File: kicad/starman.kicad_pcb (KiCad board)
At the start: 4 copper layers, 182 x 150 mm, 202 parts, among them J1 Conn_01x12, J10 Barrel_Jack_MountingPin, J2 Conn_01x10, J3 Conn_01x12, J4 Conn_01x06, J5 Conn_02x03_Counter_Clockwise, J6 Conn_01x12, J7 Conn_01x10, J8 Conn_01x12, J9 Conn_01x08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

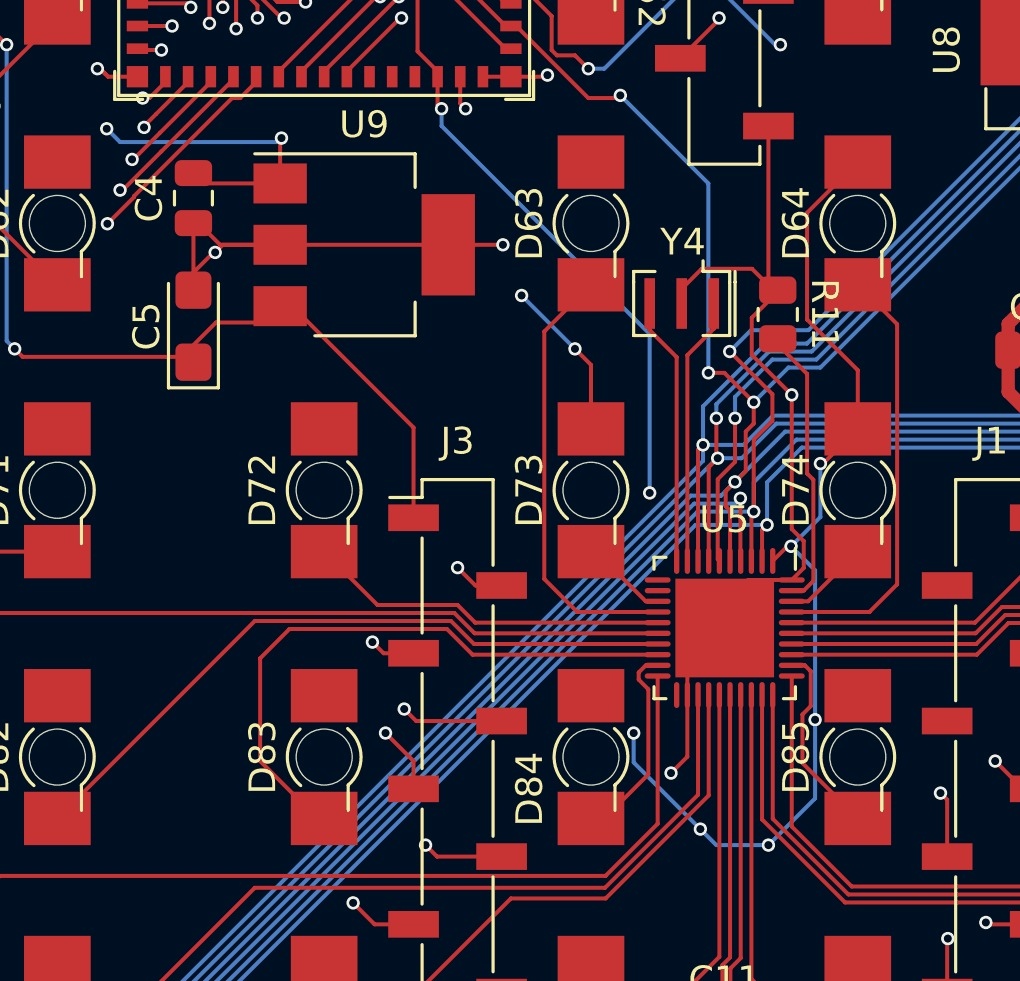
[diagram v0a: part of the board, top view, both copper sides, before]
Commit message: Clean up some +5V routes to be more balanced around D64 and D83
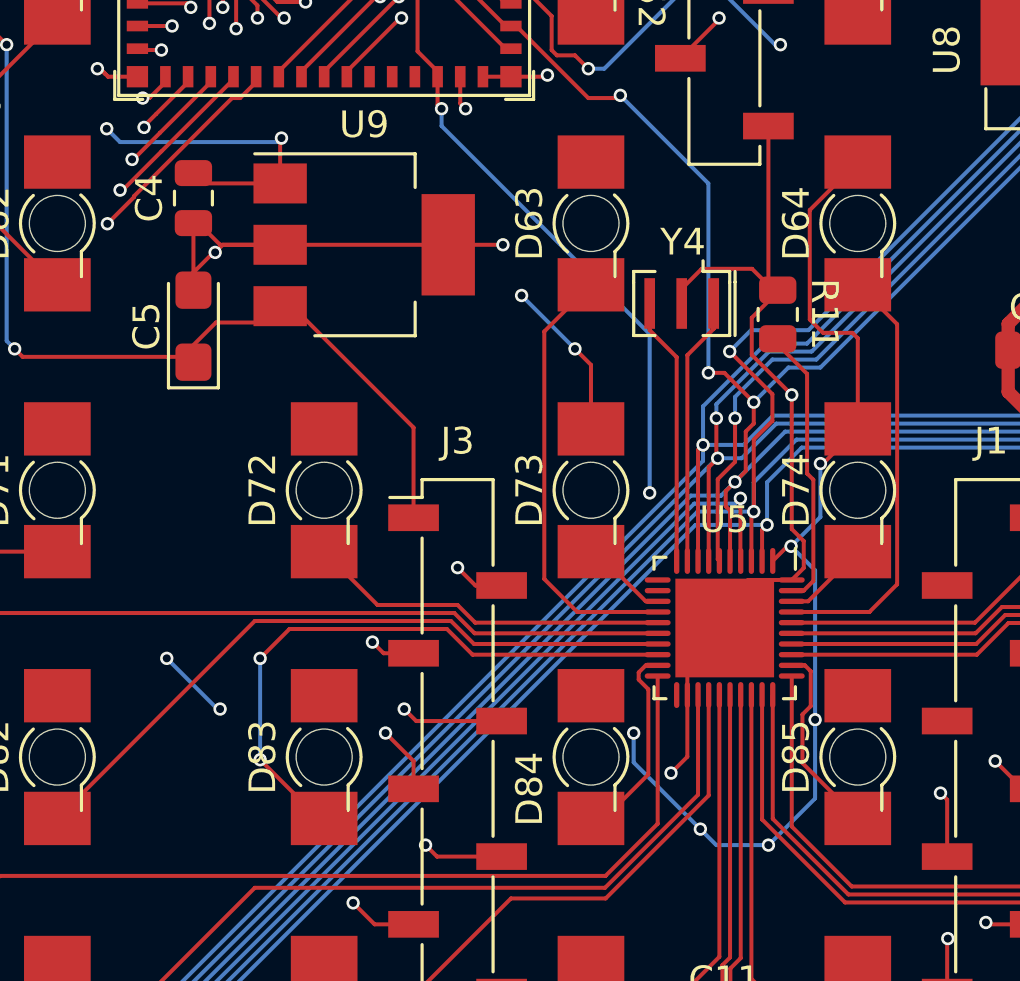
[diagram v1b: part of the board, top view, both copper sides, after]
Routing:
- net +5V: track 248.5 -> 251.9 mm, vias 50 -> 52
- net Net-(D83-Pad1): track 22.9 -> 23.2 mm, vias 0 -> 2
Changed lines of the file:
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@@
   (segment (start 165 152.7) (end 164.5 153.2) (width 0.15) (layer "F.Cu") (net 5))
   (segment (start 105 72.7) (end 106.8 74.5) (width 0.15) (layer "F.Cu") (net 5))
+  (segment (start 113.2 104.5) (end 115 102.7) (width 0.15) (layer "F.Cu") (net 5))
   (segment (start 125 132.7) (end 125 131.45) (width 0.15) (layer "F.Cu") (net 5))
   (segment (start 146.6 87.4) (end 147.3625 88.1625) (width 0.15) (layer "F.Cu") (net 5))
@@
   (segment (start 108.1 73.300794) (end 107.948511 73.452283) (width 0.15) (layer "F.Cu") (net 5))
   (segment (start 85 92.7) (end 83.9 92.7) (width 0.15) (layer "F.Cu") (net 5))
-  (segment (start 113.1 108.6) (end 113.1 104.6) (width 0.15) (layer "F.Cu") (net 5))
-  (segment (start 115 112.7) (end 115 110.5) (width 0.15) (layer "F.Cu") (net 5))
   (segment (start 145 82.7) (end 146.6 84.3) (width 0.15) (layer "F.Cu") (net 5))
   (segment (start 66.6 144.1) (end 65.2 142.7) (width 0.15) (layer "F.Cu") (net 5))
+  (segment (start 115 109.3) (end 114.8 109.1) (width 0.15) (layer "F.Cu") (net 5))
   (segment (start 162.2875 147) (end 161.8 147.4875) (width 0.15) (layer "F.Cu") (net 5))
   (segment (start 80.9875 95.075) (end 80.9875 97.5875) (width 0.15) (layer "F.Cu") (net 5))
@@
   (segment (start 80.9875 94.3125) (end 81.6 93.7) (width 0.15) (layer "F.Cu") (net 5))
   (segment (start 90.4875 103.5) (end 90.1 103.1125) (width 0.15) (layer "F.Cu") (net 5))
+  (segment (start 114.8 109.1) (end 113.7 109.1) (width 0.15) (layer "F.Cu") (net 5))
   (segment (start 61.8 147.1) (end 62.3 146.6) (width 0.15) (layer "F.Cu") (net 5))
   (segment (start 115 112.7) (end 113.7 114) (width 0.15) (layer "F.Cu") (net 5))
@@
   (segment (start 158.8125 95.9875) (end 159.6 95.2) (width 0.15) (layer "F.Cu") (net 5))
   (segment (start 145 82.7) (end 146.1 82.7) (width 0.15) (layer "F.Cu") (net 5))
+  (segment (start 113.2 108.6) (end 113.2 104.5) (width 0.15) (layer "F.Cu") (net 5))
   (segment (start 129.85 109.8) (end 127.54 107.49) (width 0.5) (layer "F.Cu") (net 5))
-  (segment (start 115 110.5) (end 113.1 108.6) (width 0.15) (layer "F.Cu") (net 5))
   (segment (start 93.35 103.5) (end 90.4875 103.5) (width 0.15) (layer "F.Cu") (net 5))
   (segment (start 112.3625 117.1) (end 112.5 117.1) (width 0.15) (layer "F.Cu") (net 5))
   (segment (start 165 92.7) (end 162.3 92.7) (width 0.15) (layer "F.Cu") (net 5))
   (segment (start 105 110.3) (end 104.4 109.7) (width 0.15) (layer "F.Cu") (net 5))
+  (segment (start 113.7 109.1) (end 113.2 108.6) (width 0.15) (layer "F.Cu") (net 5))
   (segment (start 80.9875 95.075) (end 80.9875 94.3125) (width 0.15) (layer "F.Cu") (net 5))
-  (segment (start 113.1 104.6) (end 115 102.7) (width 0.15) (layer "F.Cu") (net 5))
   (segment (start 115 72.7) (end 113.3 72.7) (width 0.15) (layer "F.Cu") (net 5))
+  (segment (start 115 112.7) (end 115 109.3) (width 0.15) (layer "F.Cu") (net 5))
   (segment (start 108.1 72.6625) (end 108.1 73.300794) (width 0.15) (layer "F.Cu") (net 5))
   (segment (start 127.54 107.49) (end 127.54 104.275) (width 0.5) (layer "F.Cu") (net 5))
@@
   (via (at 111.65 128.3) (size 0.5) (drill 0.3) (layers "F.Cu" "B.Cu") (net 5))
   (via (at 118.8 72.9) (size 0.5) (drill 0.3) (layers "F.Cu" "B.Cu") (net 5))
+  (via (at 91.1 123.2) (size 0.5) (drill 0.3) (layers "F.Cu" "B.Cu") (net 5))
   (via (at 162.3 147) (size 0.5) (drill 0.3) (layers "F.Cu" "B.Cu") (net 5))
+  (via (at 89.1 121.3) (size 0.5) (drill 0.3) (layers "F.Cu" "B.Cu") (net 5))
   (via (at 115.734095 79.565905) (size 0.5) (drill 0.3) (layers "F.Cu" "B.Cu") (net 5))
   (via (at 163.5 153.2) (size 0.5) (drill 0.3) (layers "F.Cu" "B.Cu") (net 5))
@@
   (segment (start 118.7 72.8) (end 118.8 72.9) (width 0.15) (layer "B.Cu") (net 5))
   (segment (start 113.2 77.1) (end 115.665905 79.565905) (width 0.15) (layer "B.Cu") (net 5))
+  (segment (start 91 123.2) (end 91.1 123.2) (width 0.15) (layer "B.Cu") (net 5))
   (segment (start 162.3 147) (end 162.3 145.1) (width 0.15) (layer "B.Cu") (net 5))
   (segment (start 82.6255 99.2255) (end 82.6255 100.6) (width 0.15) (layer "B.Cu") (net 5))
@@
   (segment (start 109.1 127.7) (end 106.6 125.2) (width 0.15) (layer "B.Cu") (net 5))
   (segment (start 63.2 157.3) (end 61.3 159.2) (width 0.15) (layer "B.Cu") (net 5))
+  (segment (start 89.1 121.3) (end 91 123.2) (width 0.15) (layer "B.Cu") (net 5))
   (segment (start 111.9 98.3) (end 112.1 98.3) (width 0.15) (layer "B.Cu") (net 5))
   (segment (start 63.2 147.1) (end 63.2 153.1) (width 0.15) (layer "B.Cu") (net 5))
@@
   (segment (start 100.615358 120.7625) (end 99.753347 119.900491) (width 0.15) (layer "F.Cu") (net 88))
   (segment (start 107.5 120.7625) (end 100.615358 120.7625) (width 0.15) (layer "F.Cu") (net 88))
-  (segment (start 92.6 121.3) (end 92.6 125.15) (width 0.15) (layer "F.Cu") (net 89))
-  (segment (start 92.6 125.15) (end 94.75 127.3) (width 0.15) (layer "F.Cu") (net 89))
   (segment (start 94.75 127.3) (end 95 127.3) (width 0.15) (layer "F.Cu") (net 89))
   (segment (start 99.6 120.2) (end 93.7 120.2) (width 0.15) (layer "F.Cu") (net 89))
   (segment (start 107.5 121.1625) (end 100.5625 121.1625) (width 0.15) (layer "F.Cu") (net 89))
+  (segment (start 92.6 125.1) (end 94.8 127.3) (width 0.15) (layer "F.Cu") (net 89))
   (segment (start 100.5625 121.1625) (end 99.6 120.2) (width 0.15) (layer "F.Cu") (net 89))
   (segment (start 93.7 120.2) (end 92.6 121.3) (width 0.15) (layer "F.Cu") (net 89))
+  (segment (start 94.8 127.3) (end 95 127.3) (width 0.15) (layer "F.Cu") (net 89))
+  (via (at 92.6 125.1) (size 0.5) (drill 0.3) (layers "F.Cu" "B.Cu") (net 89))
+  (via (at 92.6 121.3) (size 0.5) (drill 0.3) (layers "F.Cu" "B.Cu") (net 89))
+  (segment (start 92.6 125.1) (end 92.6 125.15) (width 0.15) (layer "B.Cu") (net 89))
+  (segment (start 92.6 121.3) (end 92.6 125.1) (width 0.15) (layer "B.Cu") (net 89))
   (segment (start 107.5 121.5625) (end 107.05356 121.5625) (width 0.15) (layer "F.Cu") (net 90))
   (segment (start 106.78798 121.82808) (end 106.78798 122.09692) (width 0.15) (layer "F.Cu") (net 90))

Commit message: Added KiCad and OSHW logos
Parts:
- J1, J3: value Conn_01x12 -> M20-8771246
- J2: value Conn_01x10 -> M20-8770646
- J4: value Conn_01x06 -> ESW-106-44-T-S
- J6, J8: value Conn_01x12 -> ESW-112-44-T-S
- J9: value Conn_01x08 -> Conn_01x10
- LS1: value Speaker -> CVS 1708
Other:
- board text added: "v2.0"
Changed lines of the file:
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@@
   (net 255 "Net-(R13-Pad2)")
   (net 256 "/ext_SOUND")
-  (net 257 "Net-(RV1-Pad2)")
+  (net 257 "Net-(LS1-Pad2)")
   (net 258 "/SOUND")
   (net 259 "Net-(R4-Pad2)")
@@
       (effects (font (size 1 1) (thickness 0.15)))
     )
-    (fp_text value "Conn_01x12" (at 0 16.84) (layer "F.Fab")
+    (fp_text value "M20-8771246" (at 0 16.84) (layer "F.Fab")
       (effects (font (size 1 1) (thickness 0.15)))
     )
@@
       (effects (font (size 1 1) (thickness 0.15)))
     )
-    (fp_text value "Conn_01x10" (at 0 9.22) (layer "F.Fab")
+    (fp_text value "M20-8770646" (at 0 9.22) (layer "F.Fab")
       (effects (font (size 1 1) (thickness 0.15)))
     )
@@
       (net 256 "/ext_SOUND") (pinfunction "1") (pintype "passive"))
     (pad "2" thru_hole circle (at -2.54 -2.54 90) (size 1.26 1.26) (drill 0.7) (layers *.Cu *.Mask)
-      (net 257 "Net-(RV1-Pad2)") (pinfunction "2") (pintype "passive"))
+      (net 257 "Net-(LS1-Pad2)") (pinfunction "2") (pintype "passive"))
     (pad "3" thru_hole circle (at 0 -5.08 90) (size 1.26 1.26) (drill 0.7) (layers *.Cu *.Mask)
-      (net 263 "unconnected-(RV1-Pad3)") (pinfunction "3") (pintype "passive"))
+      (net 263 "unconnected-(RV1-Pad3)") (pinfunction "3") (pintype "passive+no_connect"))
     (model "${KICAD6_3DMODEL_DIR}/Potentiometer_THT.3dshapes/Potentiometer_Bourns_3339P_Vertical.wrl"
       (offset (xyz 0 0 0))
@@
       (effects (font (size 1 1) (thickness 0.15)))
     )
-    (fp_text value "Conn_01x12" (at 0 16.84) (layer "F.Fab")
+    (fp_text value "M20-8771246" (at 0 16.84) (layer "F.Fab")
       (effects (font (size 1 1) (thickness 0.15)))
     )
@@
       (effects (font (size 1 1) (thickness 0.15)))
     )
-    (fp_text value "Conn_01x08" (at 0 25.19) (layer "F.Fab")
+    (fp_text value "Conn_01x10" (at 0 25.19) (layer "F.Fab")
       (effects (font (size 1 1) (thickness 0.15)))
     )
@@
       (effects (font (size 1 1) (thickness 0.15)))
     )
-    (fp_text value "Speaker" (at 4 9) (layer "F.Fab")
+    (fp_text value "CVS 1708" (at 4 9) (layer "F.Fab")
       (effects (font (size 1 1) (thickness 0.15)))
     )
@@
       (net 234 "GNDA") (pinfunction "1") (pintype "input"))
     (pad "2" thru_hole circle (at 7.61 0 180) (size 1.6002 1.6002) (drill 1.00076) (layers *.Cu *.Mask)
-      (net 257 "Net-(RV1-Pad2)") (pinfunction "2") (pintype "input"))
+      (net 257 "Net-(LS1-Pad2)") (pinfunction "2") (pintype "input"))
     (model "${KICAD6_3DMODEL_DIR}/Buzzer_Beeper.3dshapes/MagneticBuzzer_StarMicronics_HMB-06_HMB-12.wrl"
       (offset (xyz 0 0 0))
@@
     (property "Sheetfile" "starman.kicad_sch")
     (property "Sheetname" "")
+    (property "Vendor" "M20-8771246")
     (attr through_hole)
     (fp_text reference "J6" (at 0 2.33) (layer "B.SilkS")
       (effects (font (size 1 1) (thickness 0.15)) (justify mirror))
     )
-    (fp_text value "Conn_01x12" (at 0 -30.27) (layer "B.Fab")
+    (fp_text value "ESW-112-44-T-S" (at 0 -30.27) (layer "B.Fab")
       (effects (font (size 1 1) (thickness 0.15)) (justify mirror))
     )
@@
       (effects (font (size 1 1) (thickness 0.15)) (justify mirror))
     )
-    (fp_text value "Conn_01x12" (at 0 -30.27) (layer "B.Fab")
+    (fp_text value "ESW-112-44-T-S" (at 0 -30.27) (layer "B.Fab")
       (effects (font (size 1 1) (thickness 0.15)) (justify mirror))
     )
@@
       (effects (font (size 1 1) (thickness 0.15)) (justify mirror))
     )
-    (fp_text value "Conn_01x06" (at 0 -15.03) (layer "B.Fab")
+    (fp_text value "ESW-106-44-T-S" (at 0 -15.03) (layer "B.Fab")
       (effects (font (size 1 1) (thickness 0.15)) (justify mirror))
     )
@@
     (effects (font (size 1.5 1.5) (thickness 0.3)))
   )
+  (gr_text "v2.0" (at 46 162) (layer "F.SilkS")
+    (effects (font (size 1.5 1.5) (thickness 0.3)))
+  )
   (gr_text "1  2  3  4  5  6  7  8" (at 211.4 130 270) (layer "F.SilkS")
     (effects (font (size 0.8 1.03) (thickness 0.15)))
   )
+  (gr_text "v2.0" (at 185.75 148) (layer "F.SilkS")
+    (effects (font (size 1.5 1.5) (thickness 0.3)))
+  )
   (gr_text "9  5v" (at 182.6 119.6 90) (layer "F.SilkS")

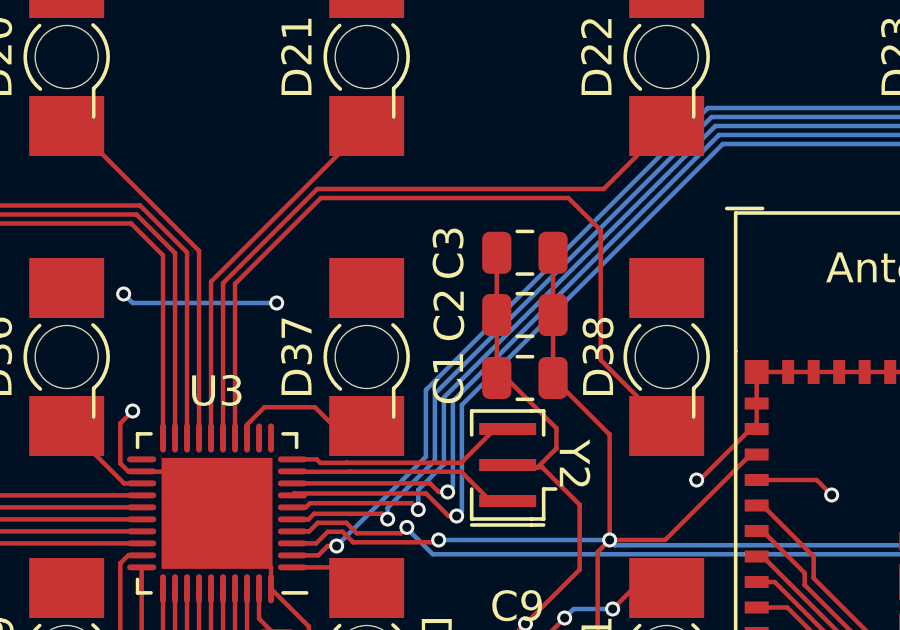
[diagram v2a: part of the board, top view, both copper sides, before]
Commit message: Properly define caps next to the 6 PCA9959 chips
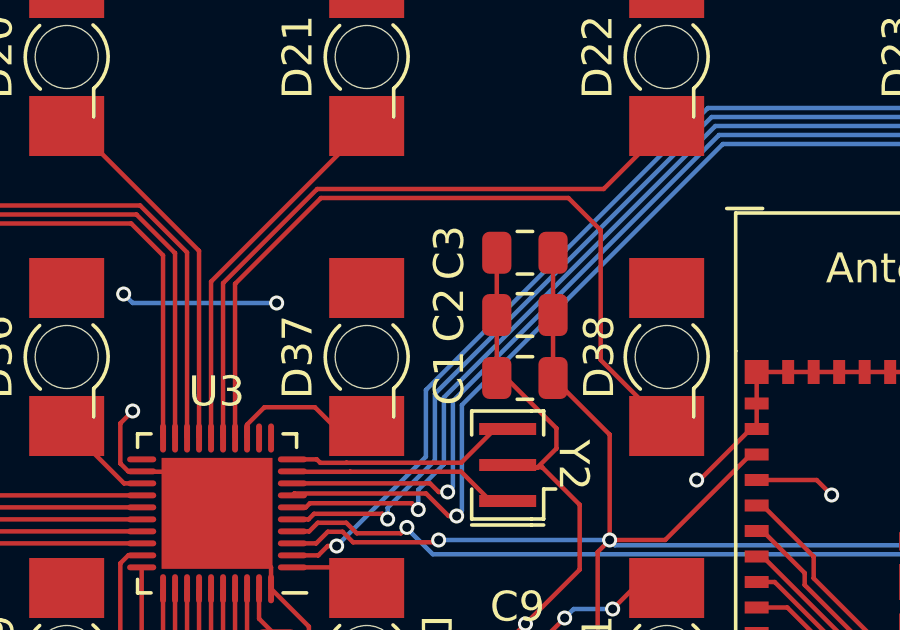
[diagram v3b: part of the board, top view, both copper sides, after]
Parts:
- C10, C11, C12, C13, C8, C9: value C -> 10uF
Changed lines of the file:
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@@
     (property "Sheetname" "")
     (attr smd)
-    (fp_text reference "C2" (at -2.5 0 90) (layer "F.SilkS")
+    (fp_text reference "C2" (at -2.525 0 90) (layer "F.SilkS")
       (effects (font (size 1 1) (thickness 0.15)))
     )
@@
       (effects (font (size 1 1) (thickness 0.15)))
     )
-    (fp_text value "C" (at 0 1.65) (layer "F.Fab")
+    (fp_text value "10uF" (at 0 1.65) (layer "F.Fab")
       (effects (font (size 1 1) (thickness 0.15)))
     )
@@
       (effects (font (size 1 1) (thickness 0.15)))
     )
-    (fp_text value "C" (at 0 1.65) (layer "F.Fab")
+    (fp_text value "10uF" (at 0 1.65) (layer "F.Fab")
       (effects (font (size 1 1) (thickness 0.15)))
     )
@@
       (effects (font (size 1 1) (thickness 0.15)))
     )
-    (fp_text value "C" (at 0 1.65) (layer "F.Fab")
+    (fp_text value "10uF" (at 0 1.65) (layer "F.Fab")
       (effects (font (size 1 1) (thickness 0.15)))
     )
@@
       (effects (font (size 1 1) (thickness 0.15)))
     )
-    (fp_text value "C" (at 0 1.65) (layer "F.Fab")
+    (fp_text value "10uF" (at 0 1.65) (layer "F.Fab")
       (effects (font (size 1 1) (thickness 0.15)))
     )
@@
       (effects (font (size 1 1) (thickness 0.15)))
     )
-    (fp_text value "C" (at 0 1.65 90) (layer "F.Fab")
+    (fp_text value "10uF" (at 0 1.65 90) (layer "F.Fab")
       (effects (font (size 1 1) (thickness 0.15)))
     )
@@
       (effects (font (size 1 1) (thickness 0.15)))
     )
-    (fp_text value "C" (at 0 1.65) (layer "F.Fab")
+    (fp_text value "10uF" (at 0 1.65) (layer "F.Fab")
       (effects (font (size 1 1) (thickness 0.15)))
     )
